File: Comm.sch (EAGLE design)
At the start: 33 parts, among them SW5 THAU13-AB-R, SW6 THAU13-AB-R, SW7 TVAF06-A020B-R, SW8 TVAF06-A020B-R, U4 OPA340N, U5 DRIVER-LV8548MC-AH(SOIC10), U6 I-02247_NJM2845

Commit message: Communication unit
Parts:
- removed U$1: LITE, TWELite:LITE
- added C1: 0.1µF, rcl:C-EUC0603K
- added TWE-LITE: LITE, TWELite:LITE
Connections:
- removed net 1: U$5.7
- removed net 2: U$5.8
- removed net 3: U$5.9
- removed net 4: U$5.10
- removed net I2C_SCL: U$2.IO22
- removed net I2C_SDA: U$2.IO21
- removed net SPI_CLK: U$2.IO18
- removed net SPI_CS: U$2.IO5
- removed net SPI_MISO: U$2.IO19
- new net TWE_!PGM!: TWE-LITE.DO1, U$5.8
- new net TWE_!RESET!: TWE-LITE.!RESET!, U$2.IO22, U$5.7
- new net TWE_!RTS!: TWE-LITE.DIO5, U$2.IO18
- new net TWE_RTX: TWE-LITE.DIO6, U$2.IO5, U$5.10
- new net TWE_SLEEP: TWE-LITE.DIO3, U$2.IO23
- new net TWE_TRX: TWE-LITE.DIO7, U$2.IO19, U$5.9
- net GND: now also C1.2, TWE-LITE.GND@1, TWE-LITE.GND@2
- net VDD: now also C1.1, TWE-LITE.VCC

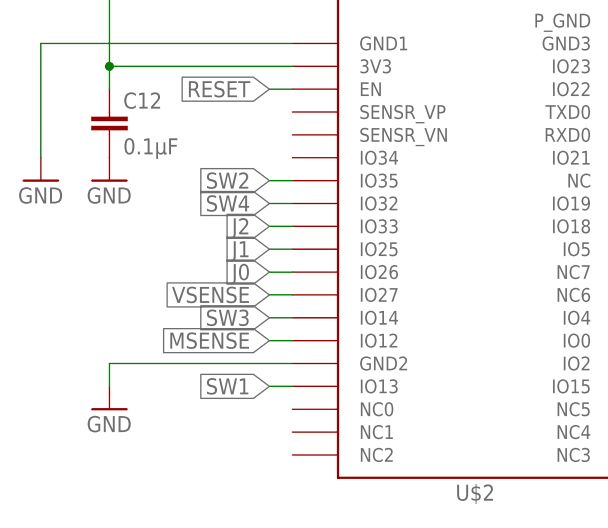
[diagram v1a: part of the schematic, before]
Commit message: Fix analog input pins
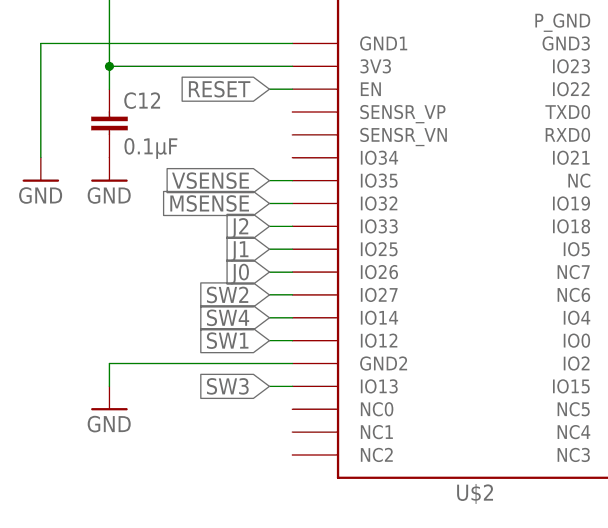
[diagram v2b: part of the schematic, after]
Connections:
- net MSENSE: now also U$2.IO32; no longer U$2.IO12
- net SW1: now also U$2.IO12; no longer U$2.IO13
- net SW2: now also U$2.IO27; no longer U$2.IO35
- net SW3: now also U$2.IO13; no longer U$2.IO14
- net SW4: now also U$2.IO14; no longer U$2.IO32
- net VSENSE: now also U$2.IO35; no longer U$2.IO27
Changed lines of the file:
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@@
 </segment>
 <segment>
-<pinref part="U$2" gate="G$1" pin="IO12"/>
-<wire x1="30.48" y1="17.78" x2="27.94" y2="17.78" width="0.1524" layer="91"/>
-<label x="27.94" y="17.78" size="1.778" layer="95" rot="R180" xref="yes"/>
+<pinref part="U$2" gate="G$1" pin="IO32"/>
+<wire x1="30.48" y1="33.02" x2="27.94" y2="33.02" width="0.1524" layer="91"/>
+<label x="27.94" y="33.02" size="1.778" layer="95" rot="R180" xref="yes"/>
 </segment>
 </net>
@@
 </segment>
 <segment>
-<pinref part="U$2" gate="G$1" pin="IO27"/>
-<wire x1="30.48" y1="22.86" x2="27.94" y2="22.86" width="0.1524" layer="91"/>
-<label x="27.94" y="22.86" size="1.778" layer="95" rot="R180" xref="yes"/>
+<pinref part="U$2" gate="G$1" pin="IO35"/>
+<wire x1="30.48" y1="35.56" x2="27.94" y2="35.56" width="0.1524" layer="91"/>
+<label x="27.94" y="35.56" size="1.778" layer="95" rot="R180" xref="yes"/>
 </segment>
 </net>
@@
 </segment>
 <segment>
-<pinref part="U$2" gate="G$1" pin="IO35"/>
-<wire x1="30.48" y1="35.56" x2="27.94" y2="35.56" width="0.1524" layer="91"/>
-<label x="27.94" y="35.56" size="1.778" layer="95" rot="R180" xref="yes"/>
+<pinref part="U$2" gate="G$1" pin="IO27"/>
+<wire x1="30.48" y1="22.86" x2="27.94" y2="22.86" width="0.1524" layer="91"/>
+<label x="27.94" y="22.86" size="1.778" layer="95" rot="R180" xref="yes"/>
 </segment>
 </net>
@@
 </segment>
 <segment>
+<pinref part="U$2" gate="G$1" pin="IO13"/>
+<wire x1="30.48" y1="12.7" x2="27.94" y2="12.7" width="0.1524" layer="91"/>
+<label x="27.94" y="12.7" size="1.778" layer="95" rot="R180" xref="yes"/>
+</segment>
+</net>
+<net name="SW4" class="0">
+<segment>
+<pinref part="SW8" gate="G$1" pin="A"/>
+<wire x1="218.44" y1="83.82" x2="215.9" y2="83.82" width="0.1524" layer="91"/>
+<label x="215.9" y="83.82" size="1.778" layer="95" rot="R180" xref="yes"/>
+</segment>
+<segment>
 <pinref part="U$2" gate="G$1" pin="IO14"/>
 <wire x1="30.48" y1="20.32" x2="27.94" y2="20.32" width="0.1524" layer="91"/>
@@
 </segment>
 </net>
-<net name="SW4" class="0">
-<segment>
-<pinref part="SW8" gate="G$1" pin="A"/>
-<wire x1="218.44" y1="83.82" x2="215.9" y2="83.82" width="0.1524" layer="91"/>
-<label x="215.9" y="83.82" size="1.778" layer="95" rot="R180" xref="yes"/>
-</segment>
-<segment>
-<pinref part="U$2" gate="G$1" pin="IO32"/>
-<wire x1="30.48" y1="33.02" x2="27.94" y2="33.02" width="0.1524" layer="91"/>
-<label x="27.94" y="33.02" size="1.778" layer="95" rot="R180" xref="yes"/>
-</segment>
-</net>
 <net name="SW1" class="0">
 <segment>
@@
 </segment>
 <segment>
-<pinref part="U$2" gate="G$1" pin="IO13"/>
-<wire x1="30.48" y1="12.7" x2="27.94" y2="12.7" width="0.1524" layer="91"/>
-<label x="27.94" y="12.7" size="1.778" layer="95" rot="R180" xref="yes"/>
-</segment>
-</net>
+<pinref part="U$2" gate="G$1" pin="IO12"/>
+<wire x1="30.48" y1="17.78" x2="27.94" y2="17.78" width="0.1524" layer="91"/>
+<label x="27.94" y="17.78" size="1.778" layer="95" rot="R180" xref="yes"/>
+</segment>
+</net>

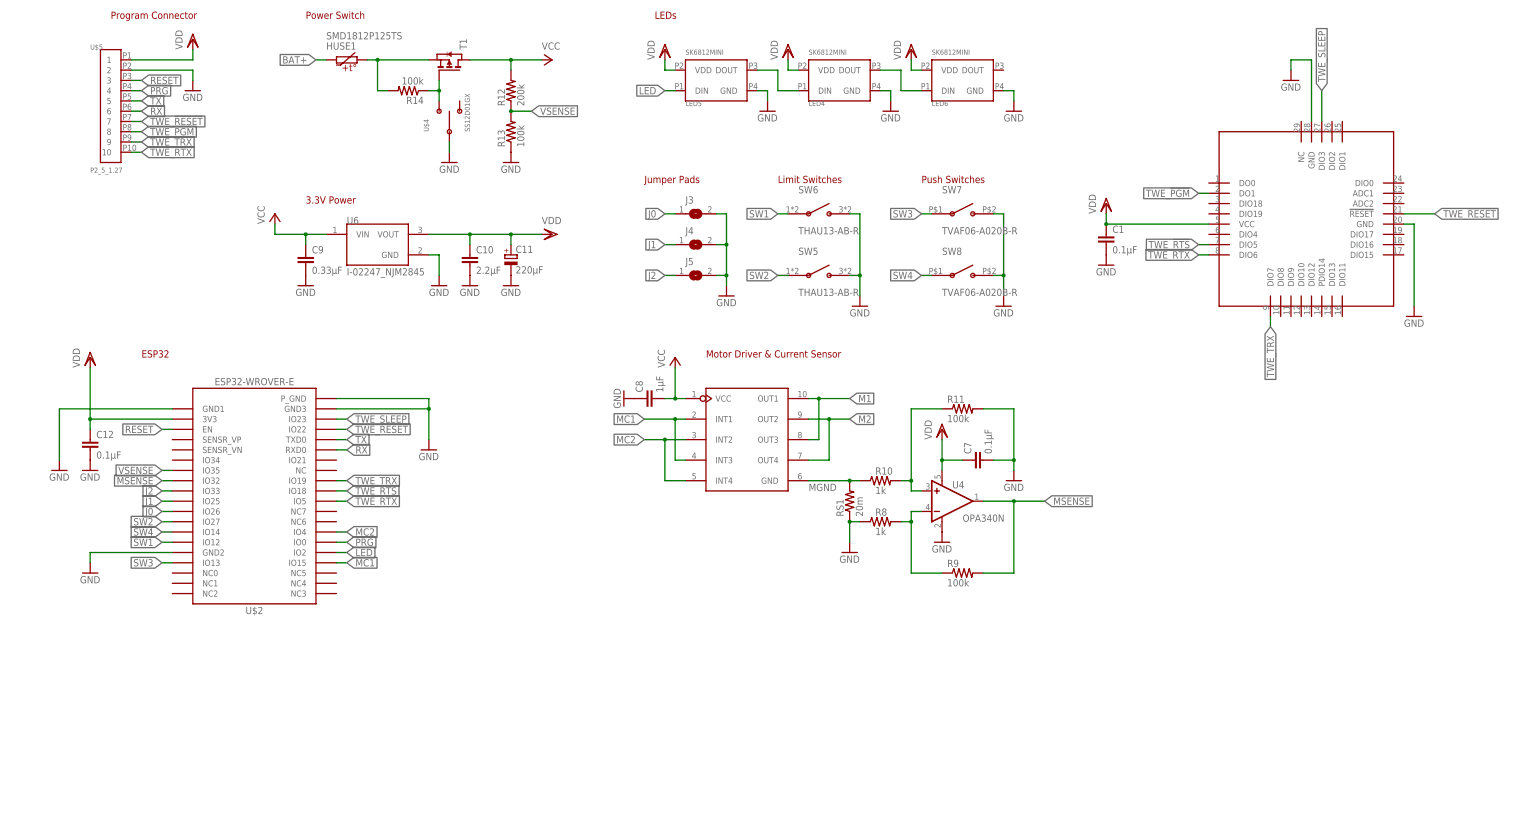
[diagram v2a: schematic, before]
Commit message: reduce switch pins
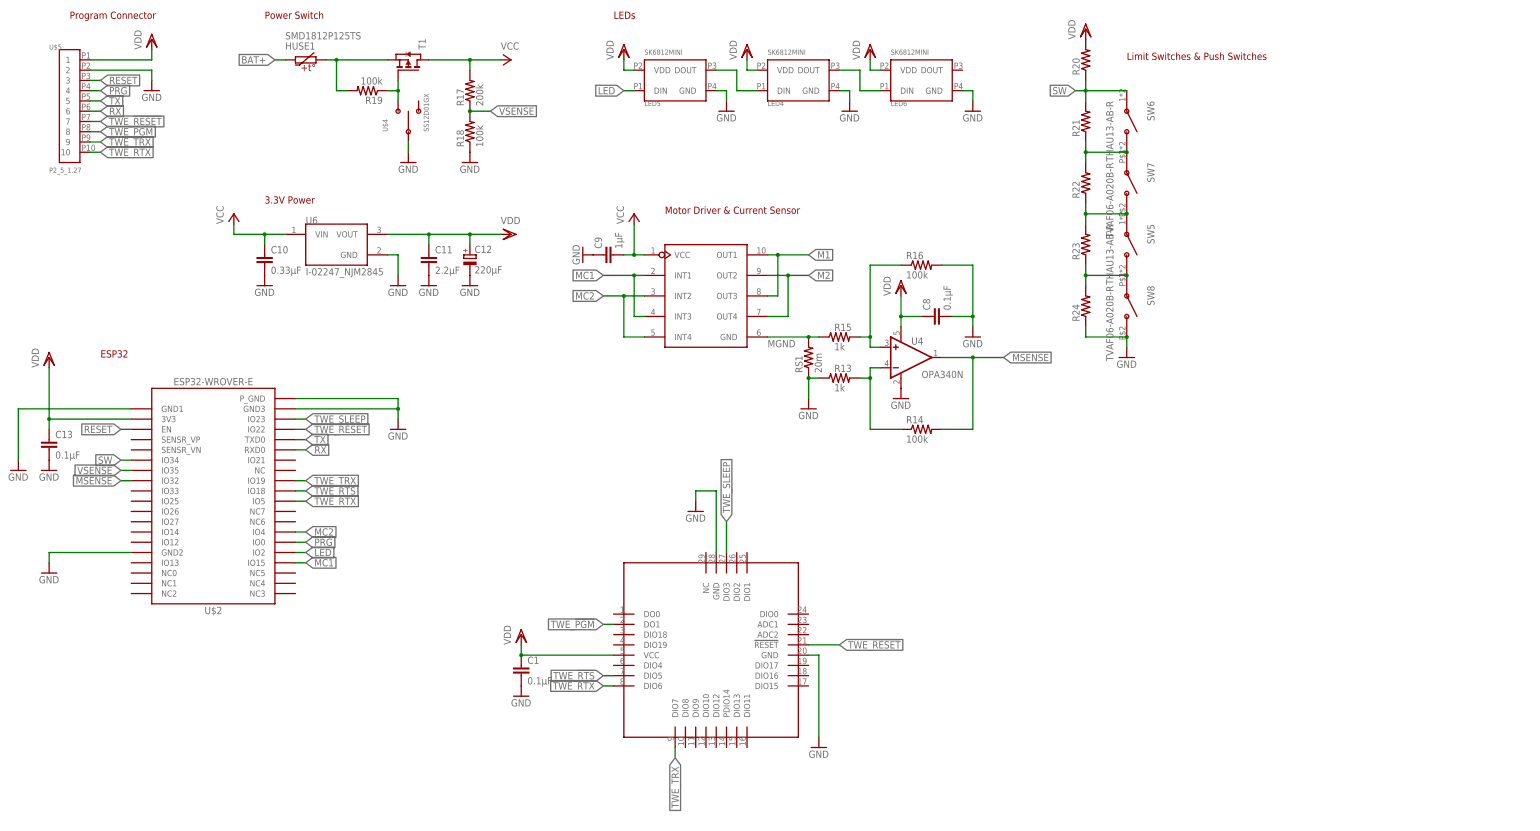
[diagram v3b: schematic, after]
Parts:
- removed C7: 0.1µF, rcl:C-EUC0603
- removed J3, J4, J5: (no value), jumper:SJ
- removed R10, R8: 1k, rcl:R-US_R0603
- removed R11, R9: 100k, rcl:R-US_R0603
- removed R12: 200k, rcl:R-US_R0603
- added C13: 0.1µF, rcl:C-EUC0603
- added R15: 1k, rcl:R-US_R0603
- added R16, R18, R19: 100k, rcl:R-US_R0603
- added R17: 200k, rcl:R-US_R0603
- added R20, R21, R22, R23, R24: (no value), rcl:R-US_R0603
- C10: value 2.2µF -> 0.33µF
- C11: value 220µF -> 2.2µF; device rcl:CPOL-EUUD-6,3X7,7 -> rcl:C-EUC0603
- C12: value 0.1µF -> 220µF; device rcl:C-EUC0603 -> rcl:CPOL-EUUD-6,3X7,7
- C8: value 1µF -> 0.1µF
- C9: value 0.33µF -> 1µF
- R13: value 100k -> 1k
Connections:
- removed net J0: J3.1, U$2.IO26
- removed net J1: J4.1, U$2.IO25
- removed net J2: J5.1, U$2.IO33
- removed net N$10: R14.1, T1.G, U$4.A
- removed net N$5: HUSE1.P2, R14.2, T1.S
- removed net N$8: R8.2, R9.1, U4.-IN
- removed net SW1: SW6.A, U$2.IO12
- removed net SW2: SW5.A, U$2.IO27
- removed net SW3: SW7.A, U$2.IO13
- removed net SW4: SW8.A, U$2.IO14
- new net N$11: R13.2, R14.1, U4.-IN
- new net N$12: R15.2, R16.1, U4.+IN
- new net N$13: R19.1, T1.G, U$4.A
- new net N$16: R22.1, R23.2, SW5.A, SW7.B
- new net N$17: R21.1, R22.2, SW6.B, SW7.A
- new net N$18: R23.1, R24.2, SW5.B, SW8.A
- new net SW: R20.1, R21.2, SW6.A, U$2.IO34
- net GND: now also C11.2, C12.-, C13.2, C8.2, C9.1, R16.2, R18.1, R24.1; no longer C11.-, C12.2, C7.2, C8.1, C9.2, J3.2, J4.2, J5.2, R11.2, R8.1, SW5.B, SW6.B, SW7.B
- net MGND: now also R15.1; no longer R10.1
- net MSENSE: now also R14.2; no longer R9.2
- net N$9: now also HUSE1.P2, R19.2, T1.S; no longer R10.2, R11.1, U4.+IN
- net VCC: now also C10.1, C9.2, R17.2; no longer C8.2, C9.1, R12.2
- net VDD: now also C11.1, C12.+, C13.1, C8.1, R20.2; no longer C10.1, C11.+, C12.1, C7.1
- net VSENSE: now also R17.1, R18.2; no longer R12.1, R13.2
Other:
- note added: "Limit Switches & Push Switches"
- note removed: "Jumper Pads"
- note removed: "Limit Switches"
- note removed: "Push Switches"
- moved on the sheet: C1, C10, C8, C9, HUSE1, LED4, LED5, LED6, R13, R14, RS1, SW5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

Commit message: change parts name
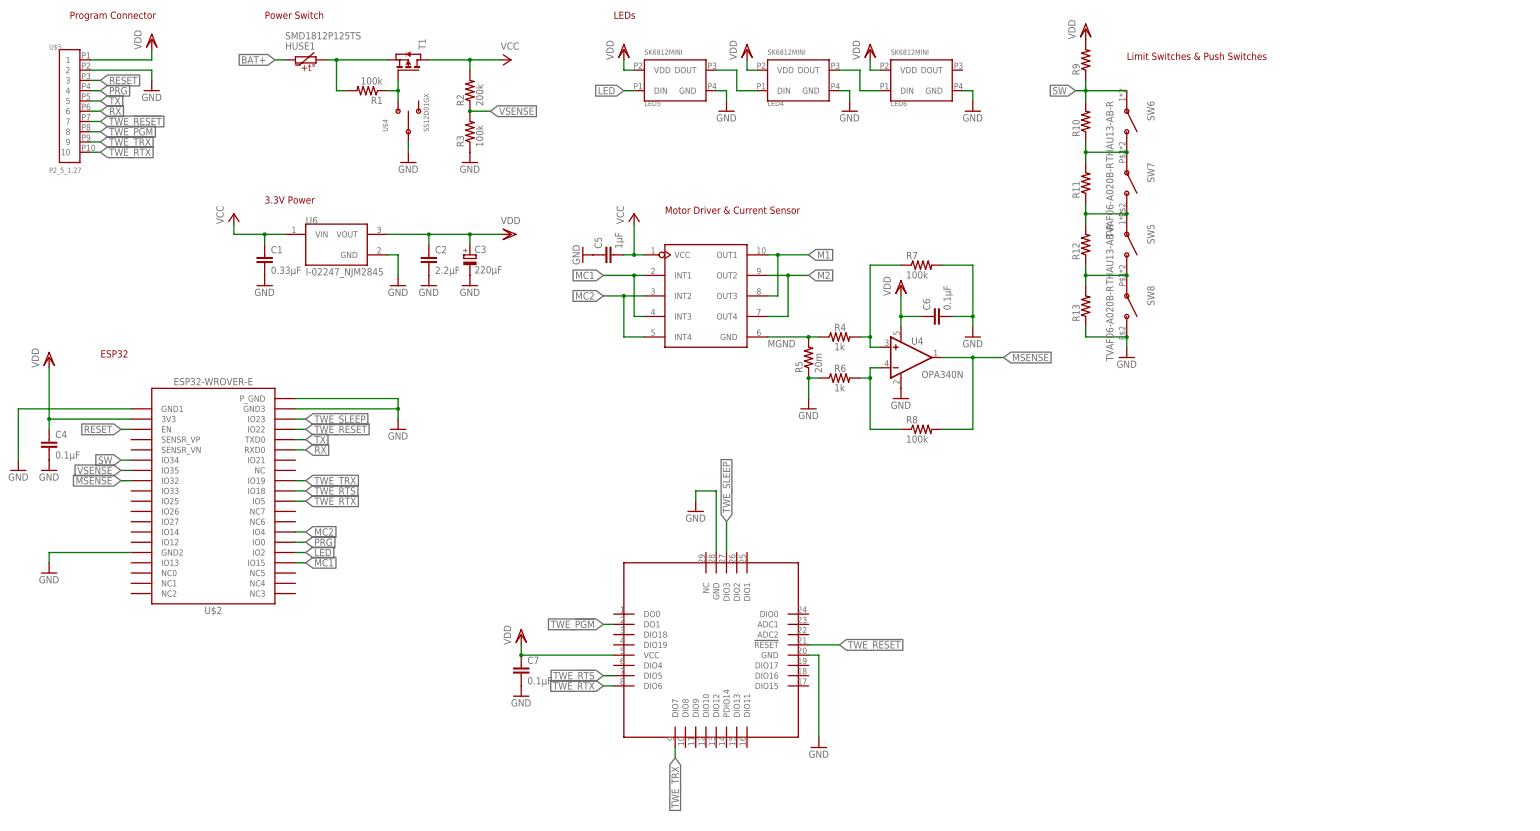
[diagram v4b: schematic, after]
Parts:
- removed C10: 0.33µF, rcl:C-EUC0603
- removed R24: (no value), rcl:R-US_R0603
- added C7: 0.1µF, rcl:C-EUC0603K
- added R6: 1k, rcl:R-US_R0603
- C1: value 0.1µF -> 0.33µF; device rcl:C-EUC0603K -> rcl:C-EUC0603
- R13: value 1k -> (none)
- renumbered C11 to C2, C12 to C3, C13 to C4, C8 to C6, C9 to C5, R14 to R8, R15 to R4, R16 to R7, R17 to R2, R18 to R3, R19 to R1, R20 to R9, R21 to R10, R22 to R11, R23 to R12, RS1 to R5
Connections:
- net GND: now also C7.2, R6.1; no longer C10.2, R24.1
- net N$11: now also R6.2; no longer R13.2
- net N$18: now also R13.2; no longer R24.2
- net VCC: now also C1.1; no longer C10.1
- net VDD: now also C7.1; no longer C1.1
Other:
- moved on the sheet: C1, R13

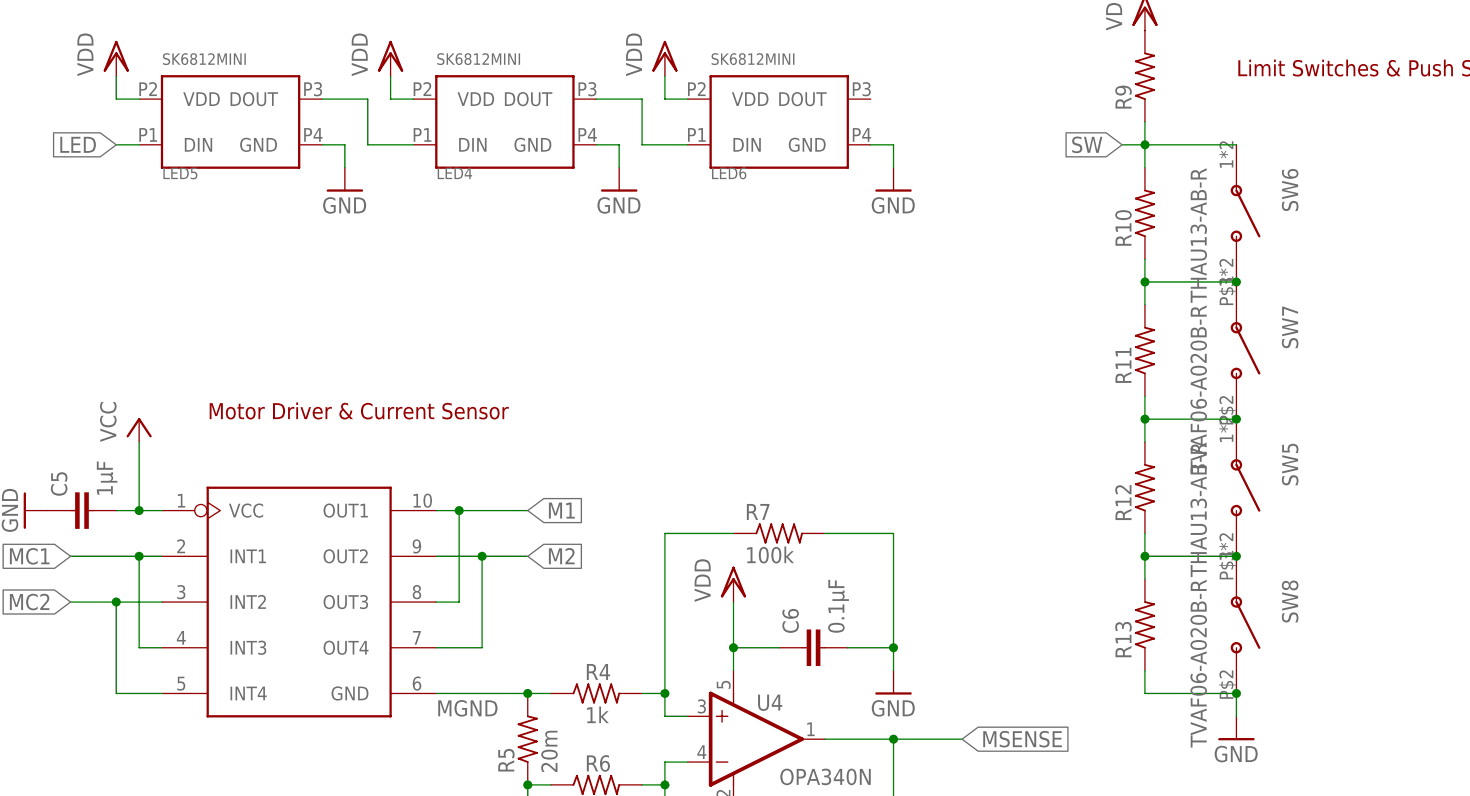
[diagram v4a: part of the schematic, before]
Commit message: Format silk
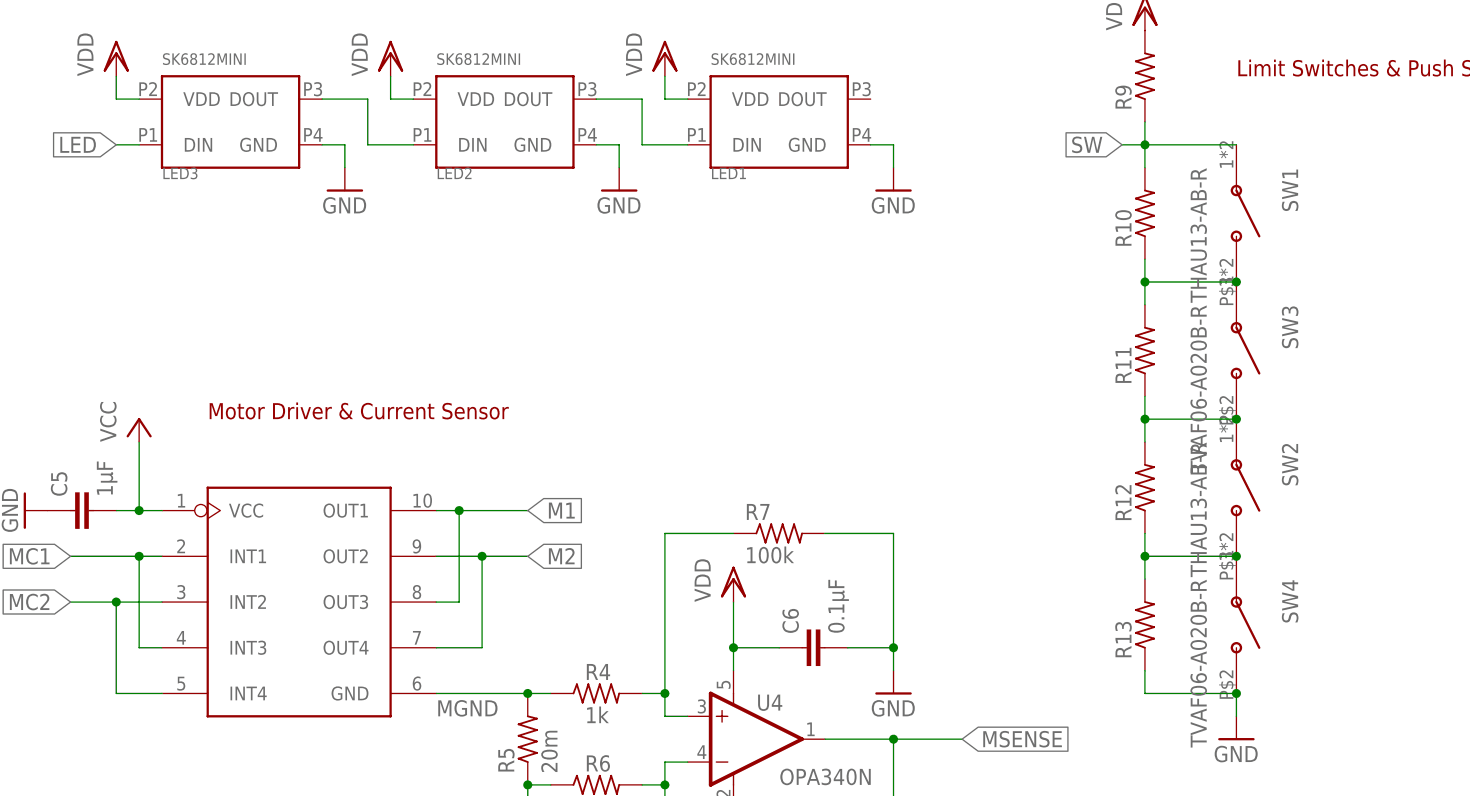
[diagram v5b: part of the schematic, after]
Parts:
- renumbered LED4 to LED2, LED5 to LED3, LED6 to LED1, SW5 to SW2, SW6 to SW1, SW7 to SW3, SW8 to SW4
